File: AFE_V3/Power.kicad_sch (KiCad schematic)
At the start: 65 parts, among them IC11 TPS7A3001DGNR, IC12 TPS7A4901DGNR, IC13 TPS72325DBVR, IC14 ADP150AUJZ-2.5-R7, IC15 ADP150AUJZ-3.3-R7, J14 TO_SWITCH, J3 DS-201, Q1 BT137S-600, U2 MDD01N-12, U3 A1215S-1WR3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

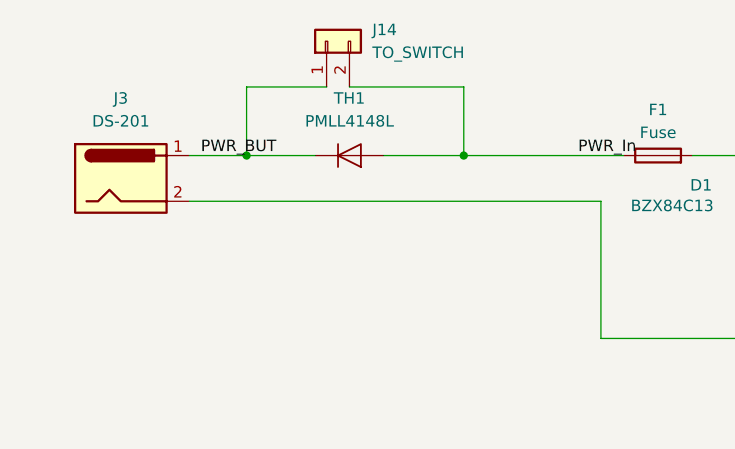
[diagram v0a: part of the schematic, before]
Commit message: PCB tracing in progress. Added some 3d models
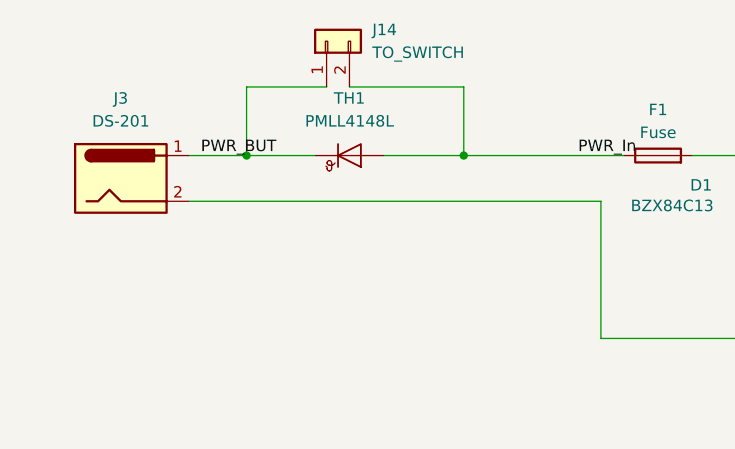
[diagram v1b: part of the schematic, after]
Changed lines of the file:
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@@
 			)
 		)
-		(property "Description" ""
+		(property "Description" "Special symbol for telling ERC where power comes from"
 			(at 261.62 78.74 0)
 			(effects
@@
 			)
 		)
-		(property "Description" ""
+		(property "Description" "Special symbol for telling ERC where power comes from"
 			(at 175.26 173.99 0)
 			(effects

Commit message: PCB tracing in progress
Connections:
- net PWR_prot: now reaches C91.1, D1.1 (A), D10.1 (A1), F1.2, F2.1, Q1.2 (A2)
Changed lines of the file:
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@@
+		)
+	)
+	(label "PWR_prot"
+		(at 133.35 31.75 0)
+		(fields_autoplaced yes)
+		(effects
+			(font
+				(size 1.27 1.27)
+			)
+			(justify left bottom)
 		)
 	)

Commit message: Added logo
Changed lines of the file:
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@@
 	(wire
 		(pts
+			(xy 123.19 140.97) (xy 128.27 140.97)
+		)
+		(stroke
+			(width 0)
+			(type default)
+		)
+	)
+	(wire
+		(pts
 			(xy 265.43 176.53) (xy 261.62 176.53)
 		)
@@
 	(wire
 		(pts
-			(xy 123.19 140.97) (xy 128.27 140.97)
-		)
-		(stroke
-			(width 0)
-			(type default)
-		)
-	)
-	(wire
-		(pts
 			(xy 173.99 130.81) (xy 186.69 130.81)
 		)
@@
 		)
 		(property "Datasheet" "http://www.st.com/content/ccc/resource/technical/document/datasheet/c9/16/86/41/c7/2b/45/f2/CD00000450.pdf/files/CD00000450.pdf/jcr:content/translations/en.CD00000450.pdf"
-			(at 45.72 229.87 0)
+			(at 45.212 222.504 0)
 			(effects
 				(font
@@
 		)
 		(property "Description" "Negative 1.5A 35V Linear Regulator, Fixed Output -5V, TO-220/TO-263"
-			(at 45.72 229.87 0)
+			(at 45.72 225.806 0)
 			(effects
 				(font
@@
 					(unit 1)
 				)
+			)
+		)
+	)
+	(symbol
+		(lib_id "power:PWR_FLAG")
+		(at 26.67 229.87 0)
+		(unit 1)
+		(exclude_from_sim no)
+		(in_bom yes)
+		(on_board yes)
+		(dnp no)
+		(fields_autoplaced yes)
+		(property "Reference" "#FLG016"
+			(at 26.67 227.965 0)
+			(effects
+				(font
+					(size 1.27 1.27)
+				)
+				(hide yes)
+			)
+		)
+		(property "Value" "PWR_FLAG"
+			(at 26.67 224.79 0)
+			(effects
+				(font
+					(size 1.27 1.27)
+				)
+			)
+		)
+		(property "Footprint" ""
+			(at 26.67 229.87 0)
+			(effects
+				(font
+					(size 1.27 1.27)
+				)
+				(hide yes)
+			)
+		)
+		(property "Datasheet" "~"
+			(at 26.67 229.87 0)
+			(effects
+				(font
+					(size 1.27 1.27)
+				)
+				(hide yes)
+			)
+		)
+		(property "Description" "Special symbol for telling ERC where power comes from"
+			(at 26.67 229.87 0)
+			(effects
+				(font
+					(size 1.27 1.27)
+				)
+				(hide yes)
+			)
+		)
+		(pin "1"
+		)
+		(instances
+			(project "AFE_V3"
+				(path "/e9ffbb94-33e2-4158-ac4a-a33b17b122cf/0098cd6c-82fc-40a6-9d9c-9293af003c7c"
+					(reference "#FLG016")
+					(unit 1)
+				)
